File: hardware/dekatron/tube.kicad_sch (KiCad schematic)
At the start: 34 parts, among them J201 TUBE_ANODE, J202 TUBE, Q201 MMBTA42, Q202 MMBTA42, Q203 MMBTA92

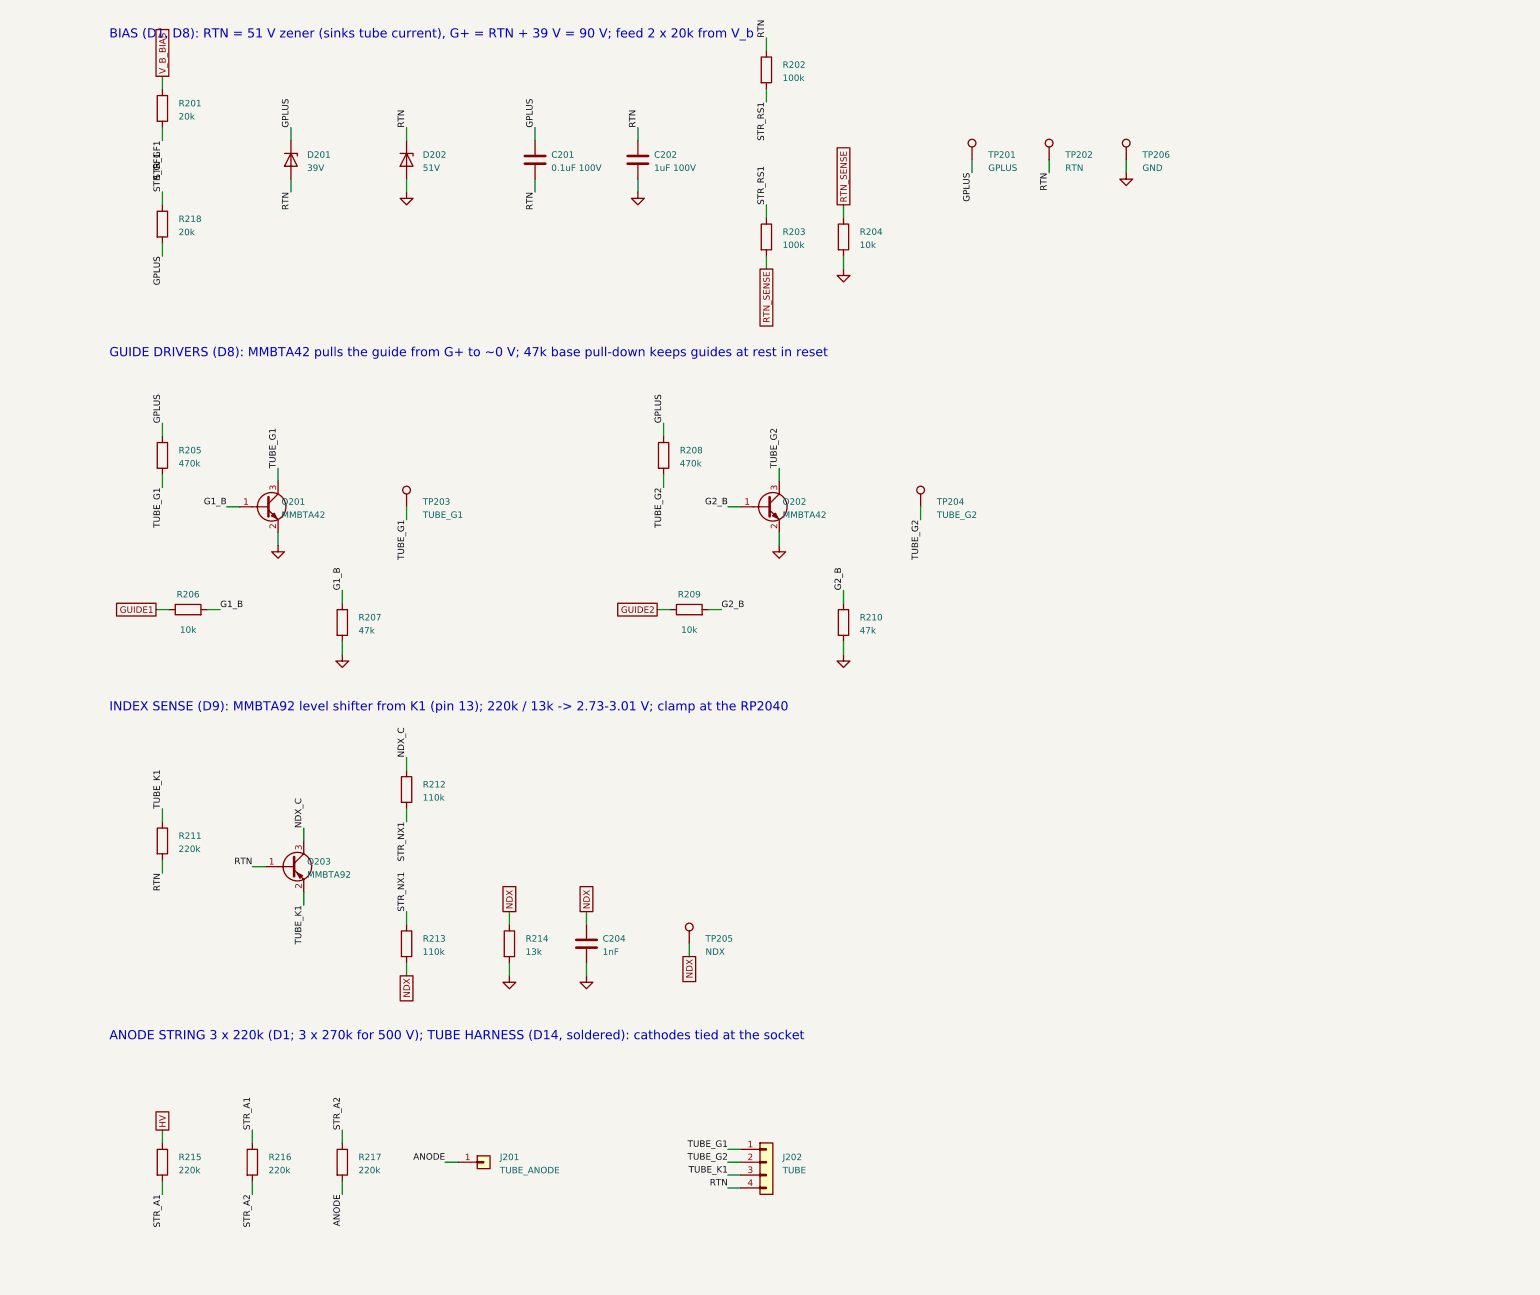
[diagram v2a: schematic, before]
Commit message: Redraw the dekatron schematics as wired, readable sheets
Each block is now drawn with real wires, power/GND symbols and junctions
instead of per-pin label stubs. Net names used by the PCB scripts and net
classes are kept as local labels; inter-sheet nets stay global labels.
Netlist pin partition verified identical to the previous version; ERC
unchanged (1 intentional LP2951/LM5156 power-output violation).

Co-Authored-By: Claude Opus 5.5 <noreply@anthropic.com>
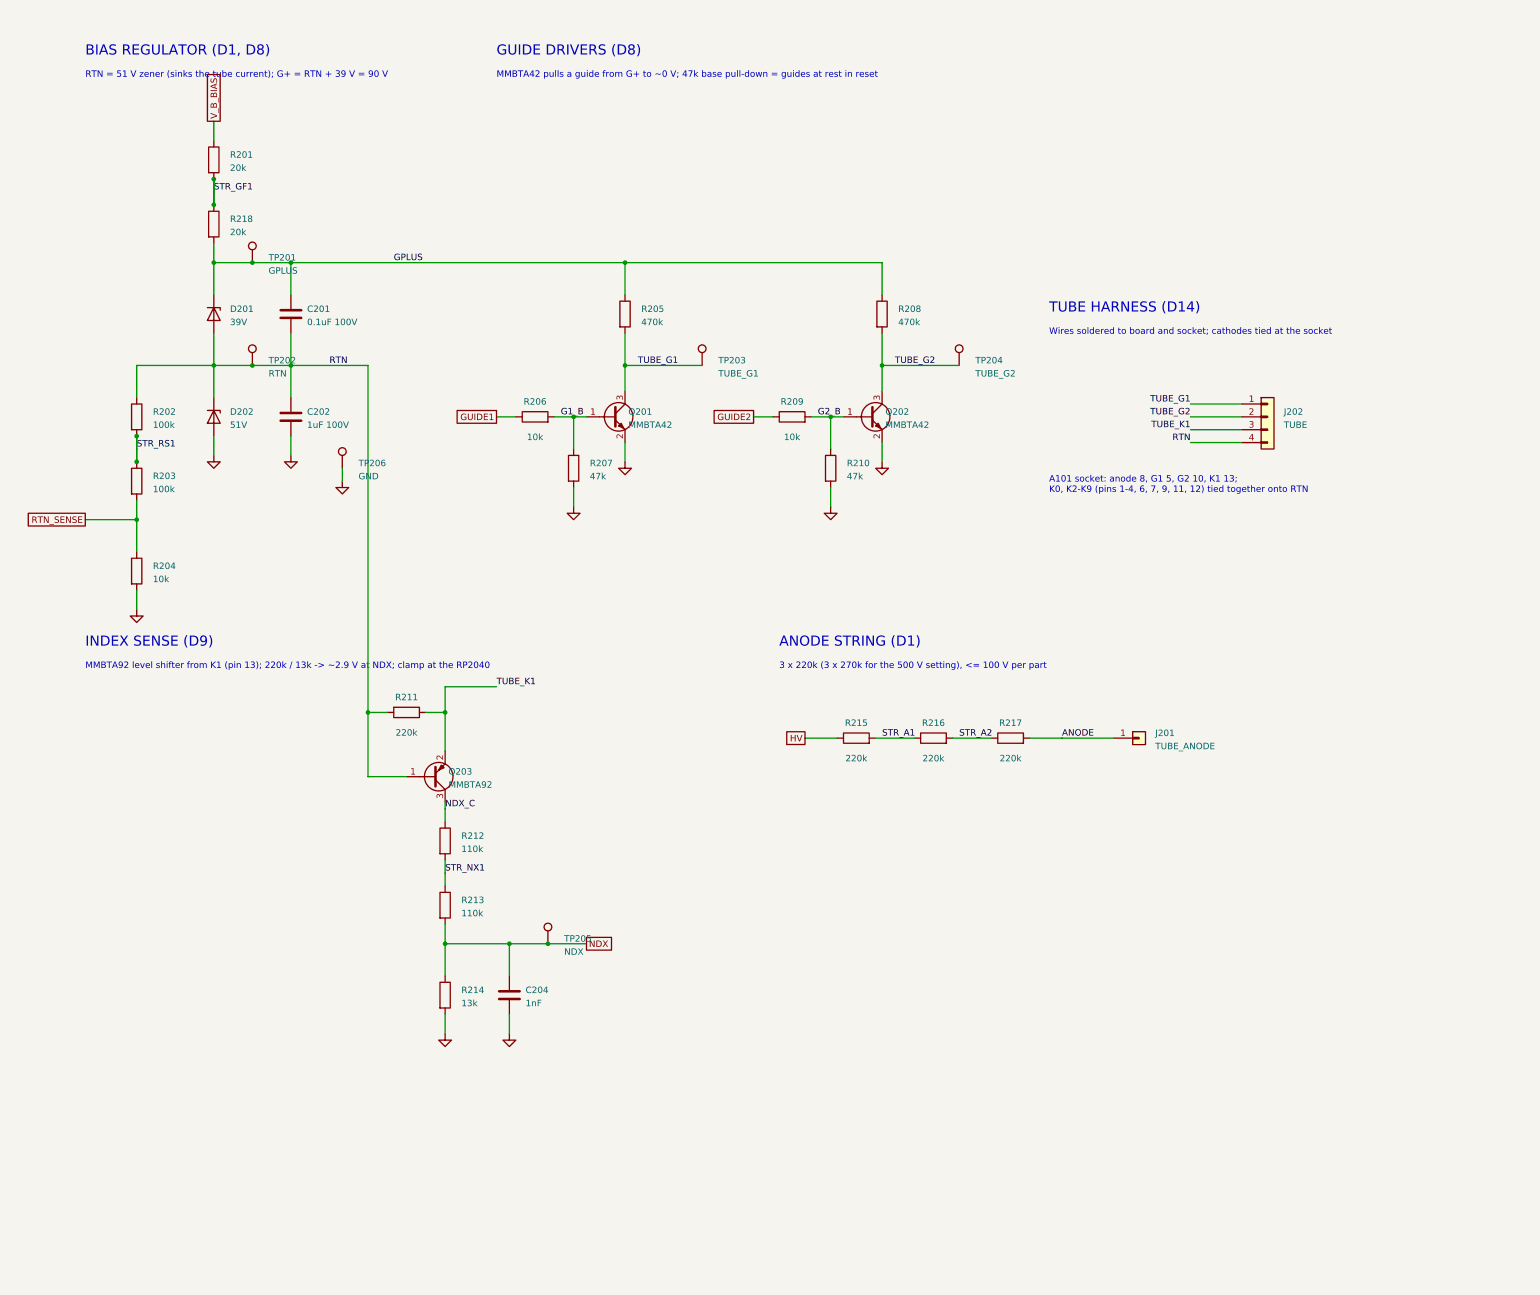
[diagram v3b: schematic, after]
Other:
- note added: "3 x 220k (3 x 270k for the 500 V setting), <= 100 V per part"
- note added: "A101 socket: anode 8, G1 5, G2 10, K1 13; K0, K2-K9 (pins 1-4, 6, 7, 9, 11, 12) tied together onto RTN"
- note added: "ANODE STRING (D1)"
- note added: "BIAS REGULATOR (D1, D8)"
- note added: "GUIDE DRIVERS (D8)"
- note added: "INDEX SENSE (D9)"
- note added: "MMBTA42 pulls a guide from G+ to ~0 V; 47k base pull-down = guides at rest in reset"
- note added: "MMBTA92 level shifter from K1 (pin 13); 220k / 13k -> ~2.9 V at NDX; clamp at the RP2040"
- note added: "RTN = 51 V zener (sinks the tube current); G+ = RTN + 39 V = 90 V"
- note added: "TUBE HARNESS (D14)"
- note added: "Wires soldered to board and socket; cathodes tied at the socket"
- note removed: "ANODE STRING 3 x 220k (D1; 3 x 270k for 500 V); TUBE HARNESS (D14, soldered): cathodes tied at the socket"
- note removed: "BIAS (D1, D8): RTN = 51 V zener (sinks tube current), G+ = RTN + 39 V = 90 V; feed 2 x 20k from V_b"
- note removed: "GUIDE DRIVERS (D8): MMBTA42 pulls the guide from G+ to ~0 V; 47k base pull-down keeps guides at rest in reset"
- note removed: "INDEX SENSE (D9): MMBTA92 level shifter from K1 (pin 13); 220k / 13k -> 2.73-3.01 V; clamp at the RP2040"
- moved on the sheet: D201, R205

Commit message: Replace 1206 HV resistor strings with single leaded HVR25/HVR37 parts
- Drop the dedicated HV bleeder; the feedback divider (HVR25 4.75M/10.5k,
  453.4 V) and a shared monitor/OVP divider (HVR25 4.64M/14.0k/10.5k,
  OVP 551.8 V, HV_SENSE = HV/190.4) discharge HV: <50 V in 1.94 s,
  3.9 s with one divider open (hv_discharge.cir).
- Dummy load: one DNP HVR37 910k. V_b bleeder/OVP, RTN_SENSE, index
  divider: single HVR25. Anode: 2 x HVR37 332k. G+/RTN feed: MRS25 40.2k.
- C304 (HV_SENSE) 100 nF -> 10 nF: on a feedback-open runaway the shared
  OVP tap lagged HV by 15.8 V with 100 nF (fault_fbopen.cir).
- BOM 180 -> 155 parts; ERC unchanged.

Co-Authored-By: Claude Opus 5.5 <noreply@anthropic.com>
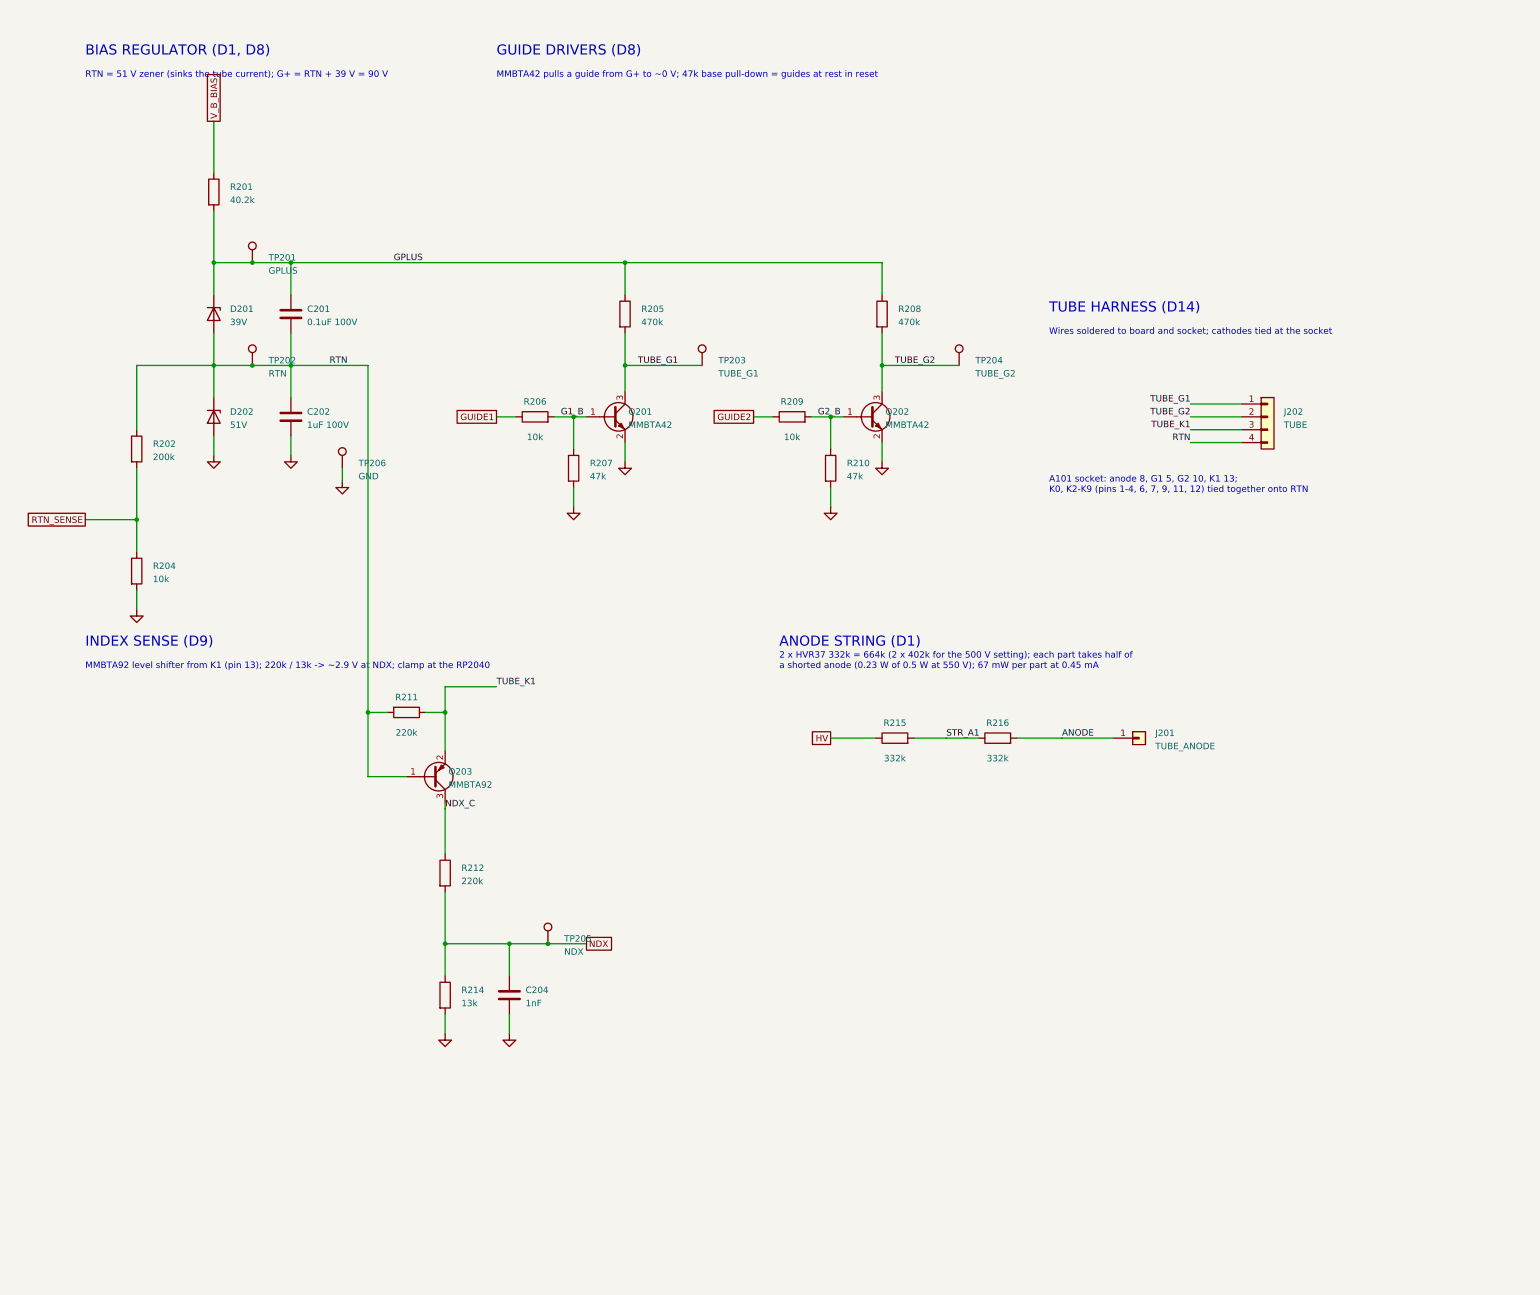
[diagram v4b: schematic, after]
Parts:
- removed R203: 100k, Resistor_SMD:R_1206_3216Metric, symbol Device:R
- removed R213: 110k, Resistor_SMD:R_1206_3216Metric, symbol Device:R
- removed R217: 220k, Resistor_SMD:R_1206_3216Metric, symbol Device:R
- removed R218: 20k, Resistor_SMD:R_1206_3216Metric, symbol Device:R
- R201: value 20k -> 40.2k; footprint Resistor_SMD:R_1206_3216Metric -> Resistor_THT:R_Axial_DIN0207_L6.3mm_D2.5mm_P10.16mm_Horizontal; Function G+ / RTN feed 1/2 (2 x 20k: 1.5-2.1 mA) -> G+ / RTN feed: 1.5-2.1 mA; 0.18 W at V_b 175 V, 0.31 W at t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; MPN (none) -> MRS25000C4022FCT00; Manufacturer (none) -> Vishay; Rating (none) -> MRS25: 0.6 W, 350 V, 1 %, 50 ppm/K
- R202: value 100k -> 200k; footprint Resistor_SMD:R_1206_3216Metric -> Resistor_THT:R_Axial_DIN0207_L6.3mm_D2.5mm_P10.16mm_Horizontal; Function RTN_SENSE divider 1/2 -> RTN_SENSE divider, upper (175 V if RTN fails to V_b); MPN (none) -> HVR2500002003FR500; Manufacturer (none) -> Vishay; Rating (none) -> HVR25: 0.25 W, 1600 V DC, 1 %, 200 ppm/K
- R212: value 110k -> 220k; footprint Resistor_SMD:R_1206_3216Metric -> Resistor_THT:R_Axial_DIN0207_L6.3mm_D2.5mm_P10.16mm_Horizontal; Function Index divider top 1/2 (167 V fault: 84 V per part) -> Index divider, upper (167 V fault); MPN (none) -> HVR2500002203FR500; Manufacturer (none) -> Vishay; Rating (none) -> HVR25: 0.25 W, 1600 V DC, 1 %, 200 ppm/K
- R215: value 220k -> 332k; footprint Resistor_SMD:R_1206_3216Metric -> Resistor_THT:R_Axial_DIN0411_L9.9mm_D3.6mm_P15.24mm_Horizontal; Function Anode resistor 1/3 (<= 100 V per part) -> Anode resistor 1/2; MPN (none) -> HVR3700003323FR500; Manufacturer (none) -> Vishay; Rating (none) -> HVR37: 0.5 W, 3500 V DC, 1 %, 200 ppm/K
- R216: value 220k -> 332k; footprint Resistor_SMD:R_1206_3216Metric -> Resistor_THT:R_Axial_DIN0411_L9.9mm_D3.6mm_P15.24mm_Horizontal; Function Anode resistor 2/3 (<= 100 V per part) -> Anode resistor 2/2; MPN (none) -> HVR3700003323FR500; Manufacturer (none) -> Vishay; Rating (none) -> HVR37: 0.5 W, 3500 V DC, 1 %, 200 ppm/K
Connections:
- net STR_A2 is gone; now on net ANODE: R216.2
- net STR_GF1 is gone; now on net GPLUS: R201.2
- net STR_NX1 is gone; now on net NDX: R212.2
- net STR_RS1 is gone; now on net RTN_SENSE: R202.2
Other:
- note added: "2 x HVR37 332k = 664k (2 x 402k for the 500 V setting); each part takes half of a shorted anode (0.23 W of 0.5 W at 550 V); 67 mW per part at 0.45 mA"
- note removed: "3 x 220k (3 x 270k for the 500 V setting), <= 100 V per part"
- moved on the sheet: R201
